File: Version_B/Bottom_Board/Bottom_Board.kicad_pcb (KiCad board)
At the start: 2 copper layers, 74.8 x 84.5 mm, 52 parts, among them J1 Conn_02x03_Top_Bottom, J2 Conn_02x03_Top_Bottom, J3 Conn_01x02_Pin, J4 Screw_Terminal_01x05, J5 DIN-5, J6 Conn_01x02_Pin, J7 Conn_01x02_Pin, J8 Screw_Terminal_01x04, SW2 SW_DIP_x04, U1 LM324, U2 LM324

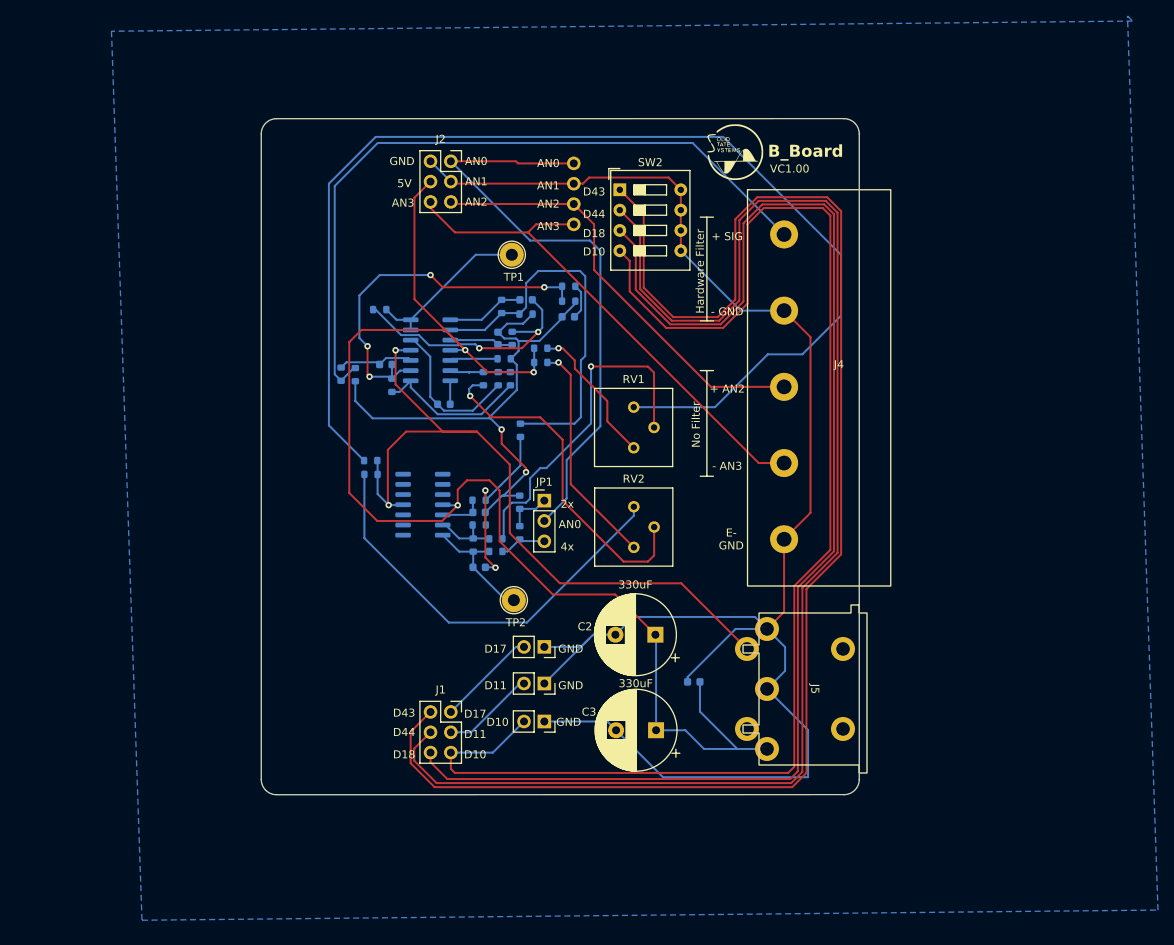
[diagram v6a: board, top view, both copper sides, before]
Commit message: 1st test for better accuracy
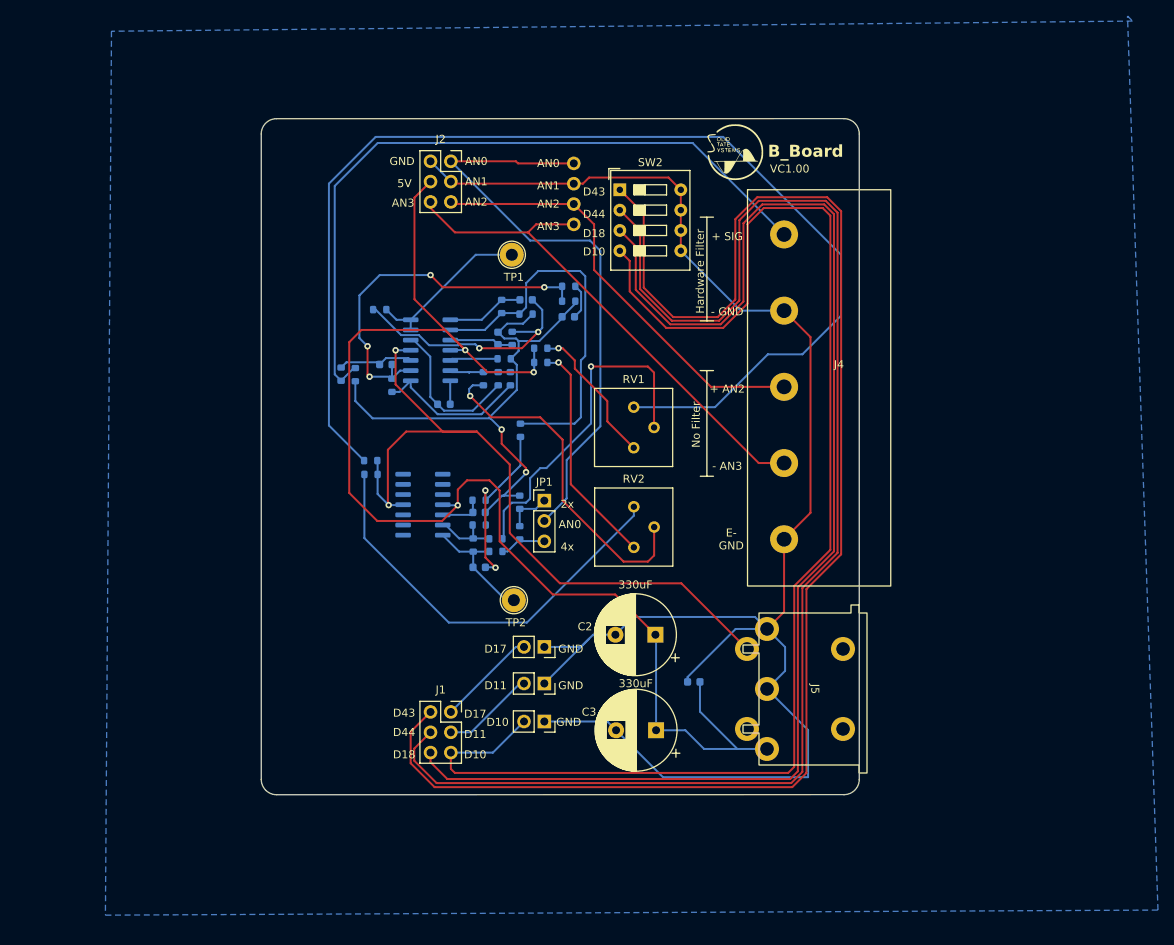
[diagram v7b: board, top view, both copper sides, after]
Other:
- board text removed: "Feather/LED Width"
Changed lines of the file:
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@@
     (effects (font (size 1 1) (thickness 0.125)) (justify left bottom))
   )
-  (gr_text "Feather/LED Width" (at 71.12 99.06 90) (layer "Dwgs.User")
-    (effects (font (size 1 1) (thickness 0.15)) (justify left bottom))
+  (dimension (type aligned) (layer "F.Cu")
+    (pts (xy 165.354 96.52) (xy 165.340651 86.958296))
+    (height -10.01476)
+    (gr_text "9.5617 mm" (at 157.132573 91.750616 -89.92000399) (layer "F.Cu")
+      (effects (font (size 1.5 1.5) (thickness 0.3)))
+    )
+    (format (prefix "") (suffix "") (units 3) (units_format 1) (precision 4))
+    (style (thickness 0.2) (arrow_length 1.27) (text_position_mode 0) (extension_height 0.58642) (extension_offset 0.5) keep_text_aligned)
   )
   (dimension (type aligned) (layer "Dwgs.User")
@@
     (height -21.918)
     (gr_text "74.7500 mm" (at 137.375 168.268) (layer "Dwgs.User")
-      (effects (font (size 1 1) (thickness 0.15)))
-    )
-    (format (prefix "") (suffix "") (units 3) (units_format 1) (precision 4))
-    (style (thickness 0.15) (arrow_length 1.27) (text_position_mode 0) (extension_height 0.58642) (extension_offset 0.5) keep_text_aligned)
-  )
-  (dimension (type aligned) (layer "Dwgs.User")
-    (pts (xy 174.75 147.5) (xy 174.752 135.382))
-    (height 5.740447)
-    (gr_text "12.1180 mm" (at 179.341447 141.441757 89.99054369) (layer "Dwgs.User")
-      (effects (font (size 1 1) (thickness 0.15)))
-    )
-    (format (prefix "") (suffix "") (units 3) (units_format 1) (precision 4))
-    (style (thickness 0.15) (arrow_length 1.27) (text_position_mode 0) (extension_height 0.58642) (extension_offset 0.5) keep_text_aligned)
-  )
-  (dimension (type aligned) (layer "Dwgs.User")
-    (pts (xy 174.752 135.255) (xy 174.752 74.295))
-    (height 33.849775)
-    (gr_text "60.9600 mm" (at 207.451775 104.775 90) (layer "Dwgs.User")
-      (effects (font (size 1 1) (thickness 0.15)))
-    )
-    (format (prefix "") (suffix "") (units 3) (units_format 1) (precision 4))
-    (style (thickness 0.15) (arrow_length 1.27) (text_position_mode 0) (extension_height 0.58642) (extension_offset 0.5) keep_text_aligned)
-  )
-  (dimension (type aligned) (layer "Dwgs.User")
-    (pts (xy 89.470013 130.935459) (xy 89.470013 80.135459))
-    (height -17.78)
-    (gr_text "50.8000 mm" (at 70.540013 105.535459 90) (layer "Dwgs.User")
       (effects (font (size 1 1) (thickness 0.15)))
     )
@@
         (xy 208.915 50.8)
         (xy 81.28 52.07)
-        (xy 85.09 163.195)
+        (xy 80.518 162.56)
         (xy 212.09 161.925)
         (xy 208.28 50.165)
@@
     )
   )
-  (group "" (id 4fb4e16f-2ab8-4827-ba31-12e19d582b0f)
-    (members
-      f7e959d5-a1b6-457c-a7fc-4cdb84e0fe1f
-      feefb24f-c8fa-4aab-b93b-243ab0c35cdf
-    )
-  )

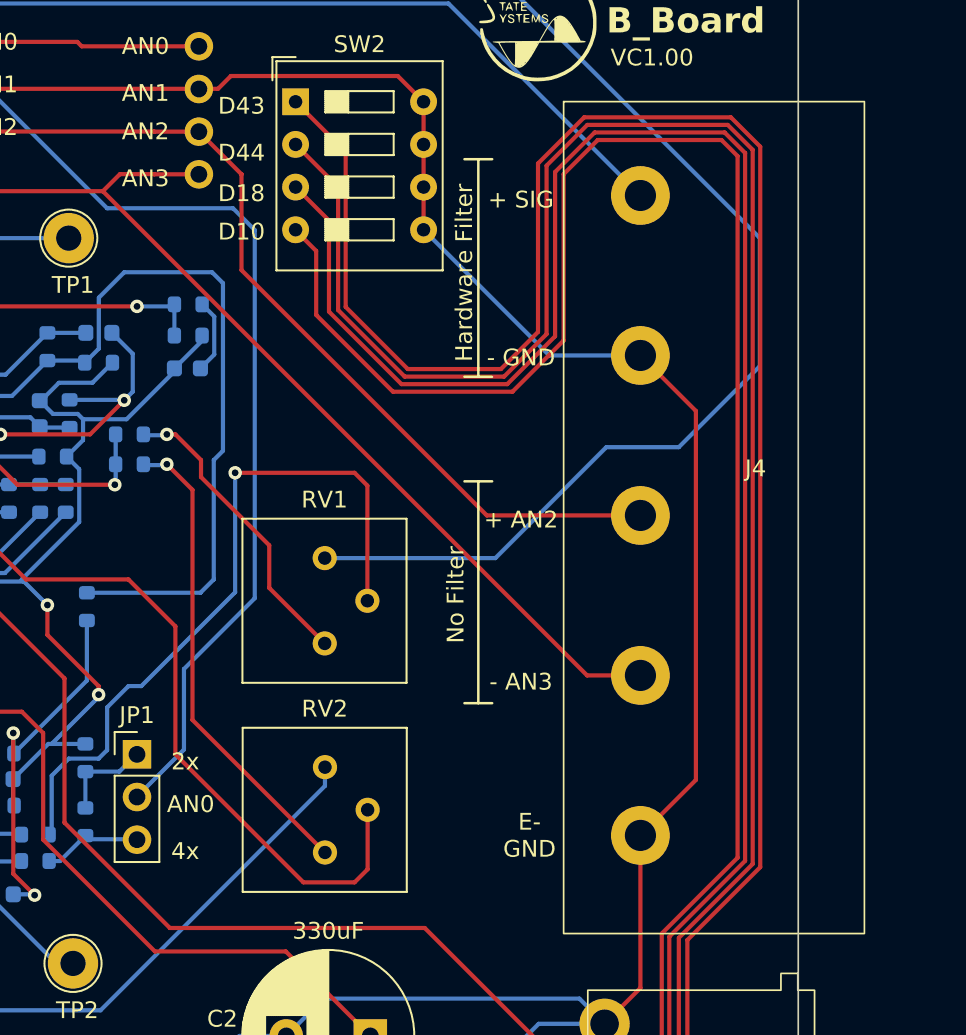
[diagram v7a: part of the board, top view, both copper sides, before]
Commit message: changed 5 pin to 4 pin term block
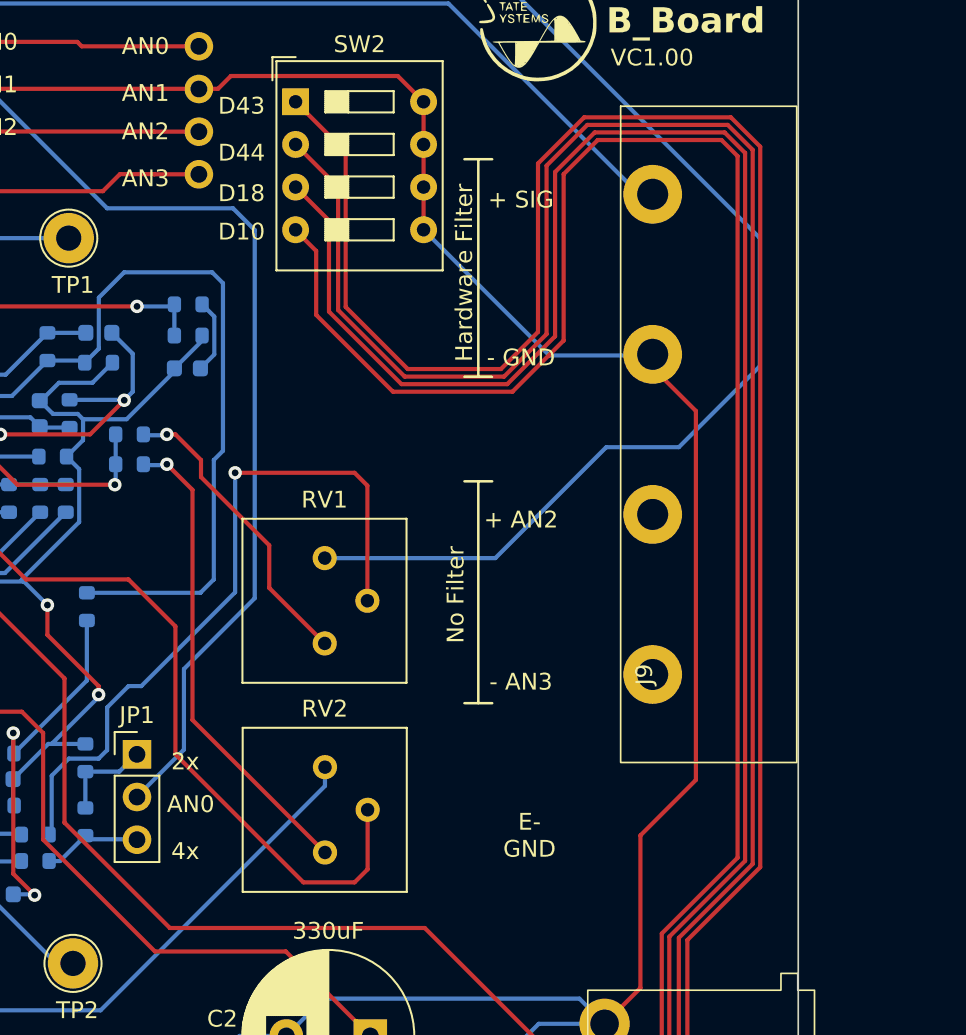
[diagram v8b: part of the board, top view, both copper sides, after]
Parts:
- removed J4: Screw_Terminal_01x05, bot_lib:BarrierStrip_1x05_P8.26mm_3.25in_Vertical
- added J9: Screw_Terminal_01x04, bot_lib:Terminal_Strip_4_Pin, F.Cu at (166.1, 106.0)
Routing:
- net AN3: track 64.3 -> 20.4 mm
- net AN2: track 54.6 -> 15.5 mm
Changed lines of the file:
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@@
-    )
-  )
-  (footprint "bot_lib:BarrierStrip_1x05_P8.26mm_3.25in_Vertical" (layer "F.Cu")
-    (at 165.354 77.47)
-    (descr "Through hole straight pin header, 1x05, 2.54mm pitch, single row")
-    (tags "Through hole pin header THT 1x05 2.54mm single row")
-    (property "Sheetfile" "Bottom_Board.kicad_sch")
-    (property "Sheetname" "")
-    (property "ki_description" "Generic screw terminal, single row, 01x05, script generated (kicad-library-utils/schlib/autogen/connector/)")
-    (property "ki_keywords" "screw terminal")
-    (attr through_hole)
-    (fp_text reference "J4" (at 6.858 16.256) (layer "F.SilkS")
-        (effects (font (size 1 1) (thickness 0.15)))
-    )
-    (fp_text value "Screw_Terminal_01x05" (at -9.525 12.8075) (layer "F.Fab") hide
-        (effects (font (size 1 1) (thickness 0.15)))
-    )
-    (fp_text user "${REFERENCE}" (at 7.62 18.288 90) (layer "F.Fab")
-        (effects (font (size 1 1) (thickness 0.15)))
-    )
-    (fp_rect (start -4.572 -5.588) (end 13.335 43.942)
-      (stroke (width 0.1) (type default)) (fill none) (layer "F.SilkS"))
-    (fp_rect (start -5.08 -6.096) (end 13.716 44.196)
-      (stroke (width 0.1) (type default)) (fill none) (layer "F.CrtYd"))
-    (pad "1" thru_hole circle (at 0 38.1) (size 3.502 3.502) (drill 1.8542) (layers "*.Cu" "*.Mask")
-      (net 3 "AN1") (pinfunction "Pin_1") (pintype "passive"))
-    (pad "2" thru_hole circle (at 0 28.575) (size 3.502 3.502) (drill 1.8542) (layers "*.Cu" "*.Mask")
-      (net 1 "AN3") (pinfunction "Pin_2") (pintype "passive"))
-    (pad "3" thru_hole circle (at 0 19.05) (size 3.502 3.502) (drill 1.8542) (layers "*.Cu" "*.Mask")
-      (net 2 "AN2") (pinfunction "Pin_3") (pintype "passive"))
-    (pad "4" thru_hole circle (at 0 9.525) (size 3.502 3.502) (drill 1.8542) (layers "*.Cu" "*.Mask")
-      (net 3 "AN1") (pinfunction "Pin_4") (pintype "passive"))
-    (pad "5" thru_hole circle (at 0 0) (size 3.502 3.502) (drill 1.8542) (layers "*.Cu" "*.Mask")
-      (net 24 "E23_INPUT") (pinfunction "Pin_5") (pintype "passive"))
-    (model "${KICAD6_3DMODEL_DIR}/Connector_PinHeader_2.54mm.3dshapes/PinHeader_1x05_P2.54mm_Vertical.wrl" hide
-      (offset (xyz 0 0 0))
-      (scale (xyz 1 1 1))
-      (rotate (xyz 0 0 0))
     )
   )
@@
       (rotate (xyz 0 0 0))
     )
+  )
+  (footprint "bot_lib:Terminal_Strip_4_Pin" (layer "F.Cu")
+    (at 166.0825 105.989 90)
+    (property "Sheetfile" "Bottom_Board.kicad_sch")
+    (property "Sheetname" "")
+    (property "ki_description" "Generic screw terminal, single row, 01x04, script generated (kicad-library-utils/schlib/autogen/connector/)")
+    (property "ki_keywords" "screw terminal")
+    (attr through_hole)
+    (fp_text reference "J9" (at 0 -0.5 90 unlocked) (layer "F.SilkS")
+        (effects (font (size 1 1) (thickness 0.1)))
+    )
+    (fp_text value "Screw_Terminal_01x04" (at 0 1 90 unlocked) (layer "F.Fab")
+        (effects (font (size 1 1) (thickness 0.15)))
+    )
+    (fp_text user "${REFERENCE}" (at 0 2.5 90 unlocked) (layer "F.Fab")
+        (effects (font (size 1 1) (thickness 0.15)))
+    )
+    (fp_rect (start 33.8315 -1.906) (end -5.2415 8.577)
+      (stroke (width 0.1) (type default)) (fill none) (layer "F.SilkS"))
+    (pad "1" thru_hole circle (at 0 0 90) (size 3.5 3.5) (drill 1.85) (layers "*.Cu" "*.Mask")
+      (net 3 "AN1") (pinfunction "Pin_1") (pintype "passive"))
+    (pad "2" thru_hole circle (at 9.53 0 90) (size 3.5 3.5) (drill 1.85) (layers "*.Cu" "*.Mask")
+      (net 3 "AN1") (pinfunction "Pin_2") (pintype "passive"))
+    (pad "3" thru_hole circle (at 19.06 0 90) (size 3.5 3.5) (drill 1.85) (layers "*.Cu" "*.Mask")
+      (net 3 "AN1") (pinfunction "Pin_3") (pintype "passive"))
+    (pad "4" thru_hole circle (at 28.59 0 90) (size 3.5 3.5) (drill 1.85) (layers "*.Cu" "*.Mask")
+      (net 24 "E23_INPUT") (pinfunction "Pin_4") (pintype "passive"))
   )
   (footprint "Potentiometer_THT:Potentiometer_Bourns_3386P_Vertical" (layer "F.Cu")
@@
     (effects (font (size 1 1) (thickness 0.125)) (justify left bottom))
   )
-  (dimension (type aligned) (layer "F.Cu")
-    (pts (xy 165.354 96.52) (xy 165.340651 86.958296))
-    (height -10.01476)
-    (gr_text "9.5617 mm" (at 157.132573 91.750616 -89.92000399) (layer "F.Cu")
-      (effects (font (size 1.5 1.5) (thickness 0.3)))
-    )
-    (format (prefix "") (suffix "") (units 3) (units_format 1) (precision 4))
-    (style (thickness 0.2) (arrow_length 1.27) (text_position_mode 0) (extension_height 0.58642) (extension_offset 0.5) keep_text_aligned)
-  )
   (dimension (type aligned) (layer "Dwgs.User")
     (pts (xy 100 147.5) (xy 100 63))
@@
   (segment (start 124.206 77.216) (end 133.35 77.216) (width 0.25) (layer "F.Cu") (net 1))
   (segment (start 134.366 76.2) (end 136.398 76.2) (width 0.25) (layer "F.Cu") (net 1))
-  (segment (start 162.179 106.045) (end 165.354 106.045) (width 0.25) (layer "F.Cu") (net 1))
-  (segment (start 133.35 77.216) (end 162.179 106.045) (width 0.25) (layer "F.Cu") (net 1))
   (segment (start 121.158 73.406) (end 121.158 74.168) (width 0.25) (layer "F.Cu") (net 1))
   (segment (start 136.408 73.67) (end 139.065 73.67) (width 0.25) (layer "F.Cu") (net 2))
-  (segment (start 141.595 76.2) (end 141.605 76.2) (width 0.25) (layer "F.Cu") (net 2))
-  (segment (start 141.605 81.915) (end 156.21 96.52) (width 0.25) (layer "F.Cu") (net 2))
   (segment (start 123.952 73.66) (end 136.398 73.66) (width 0.25) (layer "F.Cu") (net 2))
   (segment (start 123.698 73.406) (end 123.952 73.66) (width 0.25) (layer "F.Cu") (net 2))
-  (segment (start 156.21 96.52) (end 165.354 96.52) (width 0.25) (layer "F.Cu") (net 2))
   (segment (start 136.398 73.66) (end 136.408 73.67) (width 0.25) (layer "F.Cu") (net 2))
-  (segment (start 141.605 76.2) (end 141.605 81.915) (width 0.25) (layer "F.Cu") (net 2))
-  (segment (start 139.065 73.67) (end 141.595 76.2) (width 0.25) (layer "F.Cu") (net 2))
   (segment (start 140.208 71.12) (end 136.398 71.12) (width 0.25) (layer "F.Cu") (net 3))
   (segment (start 168.656 112.268) (end 168.656 90.297) (width 0.25) (layer "F.Cu") (net 3))
